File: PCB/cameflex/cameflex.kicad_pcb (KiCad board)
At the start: 2 copper layers, 1 part, among them Q1 JY317P

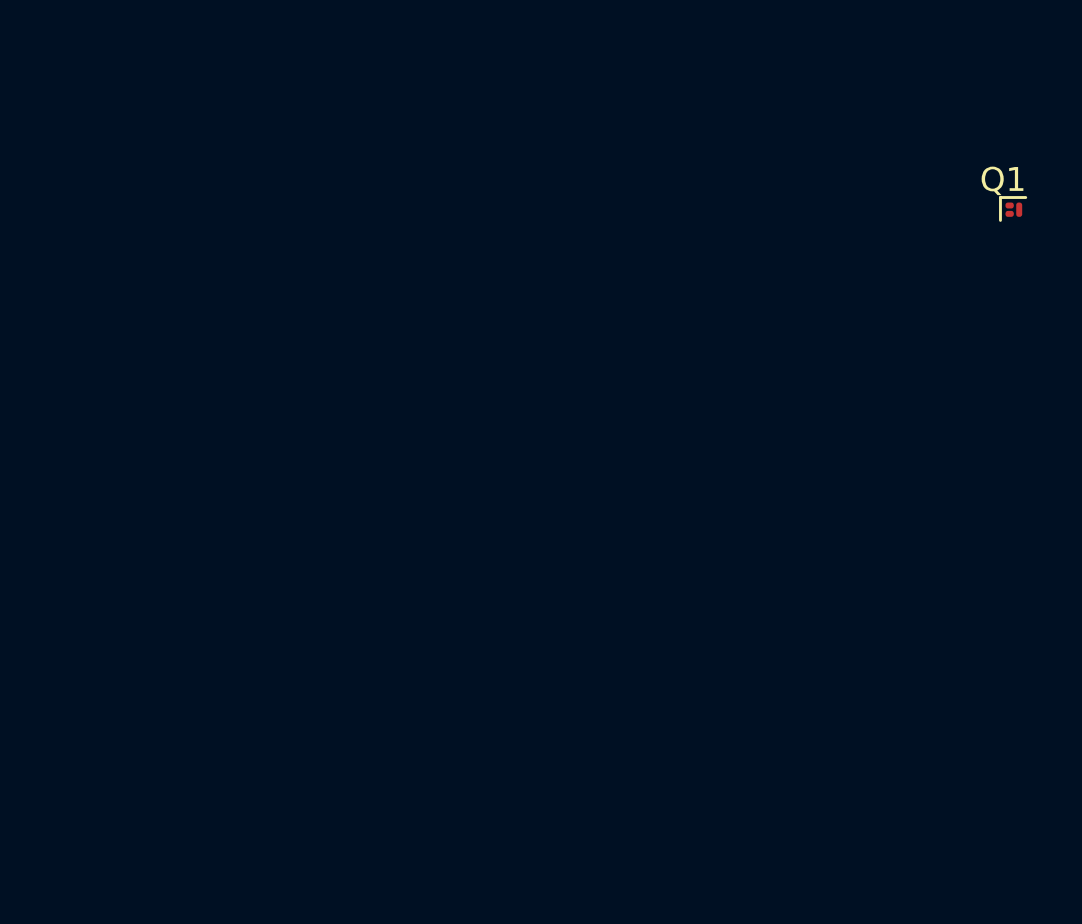
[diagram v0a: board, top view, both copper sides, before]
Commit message: Refactor Arduino Uno PID control and sensitivity trim integration
- Updated the PID control logic to allow for a sensitivity trim via a potentiometer, enhancing tuning flexibility without altering the target RPM.
- Removed obsolete potentiometer handling for target RPM and replaced it with a single sensitivity scale adjustment.
- Simplified the control loop by consolidating mode checks and updating gain calculations based on the sensitivity trim.
- Revised documentation to reflect changes in hardware setup and configuration for improved clarity and usability.
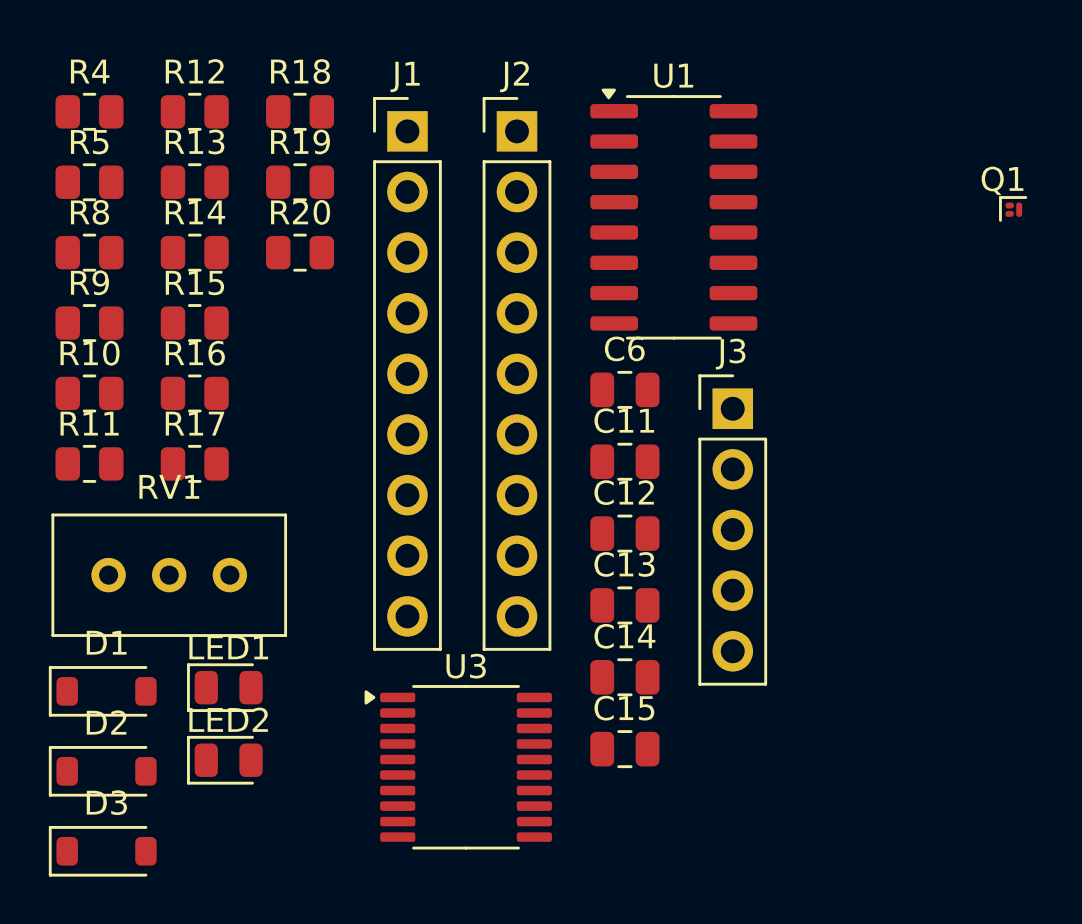
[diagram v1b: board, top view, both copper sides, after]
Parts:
- added C11: 100nF, Capacitor_SMD:C_0805_2012Metric, F.Cu at (99.0, 81.1)
- added C12: 470nF, Capacitor_SMD:C_0805_2012Metric, F.Cu at (99.0, 84.1)
- added C13: 10uF, Capacitor_SMD:C_0805_2012Metric, F.Cu at (99.0, 87.1)
- added C14: 10uF, Capacitor_SMD:C_0805_2012Metric, F.Cu at (99.0, 90.1)
- added C15: 10uF, Capacitor_SMD:C_0805_2012Metric, F.Cu at (99.0, 93.1)
- added C6: 100nF, Capacitor_SMD:C_0805_2012Metric, F.Cu at (99.0, 78.0)
- added D1: 1N4148, Diode_SMD:D_SOD-123, F.Cu at (77.3, 90.7)
- added D2: 1N4148, Diode_SMD:D_SOD-123, F.Cu at (77.3, 94.0)
- added D3: 1N4148, Diode_SMD:D_SOD-123, F.Cu at (77.3, 97.4)
- added J1: ESP32-C3_Left, Connector_PinHeader_2.54mm:PinHeader_1x09_P2.54mm_Vertical, F.Cu at (89.9, 67.2)
- added J2: ESP32-C3_Right, Connector_PinHeader_2.54mm:PinHeader_1x09_P2.54mm_Vertical, F.Cu at (94.5, 67.2)
- added J3: CON5_HALL, Connector_PinHeader_2.54mm:PinHeader_1x05_P2.54mm_Vertical, F.Cu at (103.5, 78.8)
- added LED1: PWR, LED_SMD:LED_0805_2012Metric, F.Cu at (82.4, 90.5)
- added LED2: ERR, LED_SMD:LED_0805_2012Metric, F.Cu at (82.4, 93.6)
- added R10: 100R, Resistor_SMD:R_0805_2012Metric, F.Cu at (76.5, 78.2)
- added R11: 100R, Resistor_SMD:R_0805_2012Metric, F.Cu at (76.5, 81.2)
- added R12: 100R, Resistor_SMD:R_0805_2012Metric, F.Cu at (81.0, 66.4)
- added R13: 100R, Resistor_SMD:R_0805_2012Metric, F.Cu at (81.0, 69.3)
- added R14: 15R, Resistor_SMD:R_0805_2012Metric, F.Cu at (81.0, 72.3)
- added R15: 15R, Resistor_SMD:R_0805_2012Metric, F.Cu at (81.0, 75.2)
- added R16: 15R, Resistor_SMD:R_0805_2012Metric, F.Cu at (81.0, 78.2)
- added R17: 15R, Resistor_SMD:R_0805_2012Metric, F.Cu at (81.0, 81.2)
- added R18: 15R, Resistor_SMD:R_0805_2012Metric, F.Cu at (85.4, 66.4)
- added R19: 15R, Resistor_SMD:R_0805_2012Metric, F.Cu at (85.4, 69.3)
- added R20: 560R, Resistor_SMD:R_0805_2012Metric, F.Cu at (85.4, 72.3)
- added R4: 2.2K, Resistor_SMD:R_0805_2012Metric, F.Cu at (76.5, 66.4)
- added R5: 3.3K, Resistor_SMD:R_0805_2012Metric, F.Cu at (76.5, 69.3)
- added R8: 100R, Resistor_SMD:R_0805_2012Metric, F.Cu at (76.5, 72.3)
- added R9: 100R, Resistor_SMD:R_0805_2012Metric, F.Cu at (76.5, 75.2)
- added RV1: 10K, Potentiometer_THT:Potentiometer_Bourns_3296W_Vertical, F.Cu at (82.4, 85.8)
- added U1: JY01(8559), Package_SO:SOP-16_3.9x9.9mm_P1.27mm, F.Cu at (101.0, 70.8)
- added U3: JY213L, Package_SO:TSSOP-20_4.4x6.5mm_P0.65mm, F.Cu at (92.3, 93.9)
